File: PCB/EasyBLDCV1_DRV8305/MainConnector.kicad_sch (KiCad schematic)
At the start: 14 parts, among them J1 10159560-A00221RLF, U4 LMR16006XDDCR

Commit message: Fixed Naming Scheme
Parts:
- removed J1: 10159560-A00221RLF, Connectors:AMPHENOL_10159560-A00221RLF, symbol Connectors:10159560-A00221RLF
- removed L1: 15u, symbol Device:L
- removed U4: LMR16006XDDCR, LMR16006XDDCR:DDC0006A, symbol LMR16006XDDCR:LMR16006XDDCR
- added J1: 10159560-A00221RLF, 10159560-A00221RLF:AMPHENOL_10159560-A00221RLF, symbol EasyBLDC:10159560-A00221RLF
- added L1: SD53-120-R, EasyBLDC:SD53, symbol SD53:SD53-470-R
- added U4: LMR16006XDDCR, EasyBLDC:DDC0006A, symbol EasyBLDC:LMR16006XDDCR
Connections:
- net 3.3V: now also L1.2
- net COM: now also J1.10
- net GND: now also J1.3, J1.4, J1.8, J1.9, J1.S1 (SHIELD), J1.S2 (SHIELD__1), U4.2 (GND)
- net MOT_A: now also J1.5
- net MOT_B: now also J1.6
- net MOT_C: now also J1.7
- net PVDD: now also J1.1, J1.2, U4.5 (VIN)
- net at C20.1, D1.1 (K): now also L1.1, U4.6 (SW)
- net at R15.2, R16.1: now also U4.3 (FB)
- net at C20.2: now also U4.1 (CB)

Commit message: Updated Schematic With Missing Footprints
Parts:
- C18: footprint (none) -> EasyBLDC:CAP_FP_10P3X10P3_PAN
- J1: footprint 10159560-A00221RLF:AMPHENOL_10159560-A00221RLF -> EasyBLDC:AMPHENOL_10159560-A00221RLF
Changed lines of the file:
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@@
 			)
 		)
-		(property "Footprint" ""
+		(property "Footprint" "EasyBLDC:CAP_FP_10P3X10P3_PAN"
 			(at 59.69 127 0)
 			(effects
@@
 			)
 		)
-		(property "Footprint" "10159560-A00221RLF:AMPHENOL_10159560-A00221RLF"
+		(property "Footprint" "EasyBLDC:AMPHENOL_10159560-A00221RLF"
 			(at 71.12 60.96 0)
 			(effects

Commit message: Finished Initial Layout
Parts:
- 3V3: footprint TestPoint:TestPoint_Pad_D3.0mm -> TestPoint:TestPoint_Pad_D2.0mm
- C18: value 390u -> 10u; footprint EasyBLDC:CAP_FP_10P3X10P3_PAN -> Capacitor_SMD:C_1210_3225Metric
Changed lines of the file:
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@@
 			)
 		)
-		(property "Value" "390u"
+		(property "Value" "10u"
 			(at 63.5 127.6349 0)
 			(effects
@@
 			)
 		)
-		(property "Footprint" "EasyBLDC:CAP_FP_10P3X10P3_PAN"
+		(property "Footprint" "Capacitor_SMD:C_1210_3225Metric"
 			(at 59.69 127 0)
 			(effects
@@
 			)
 		)
-		(property "Footprint" "TestPoint:TestPoint_Pad_D3.0mm"
+		(property "Footprint" "TestPoint:TestPoint_Pad_D2.0mm"
 			(at 237.49 44.45 0)
 			(effects

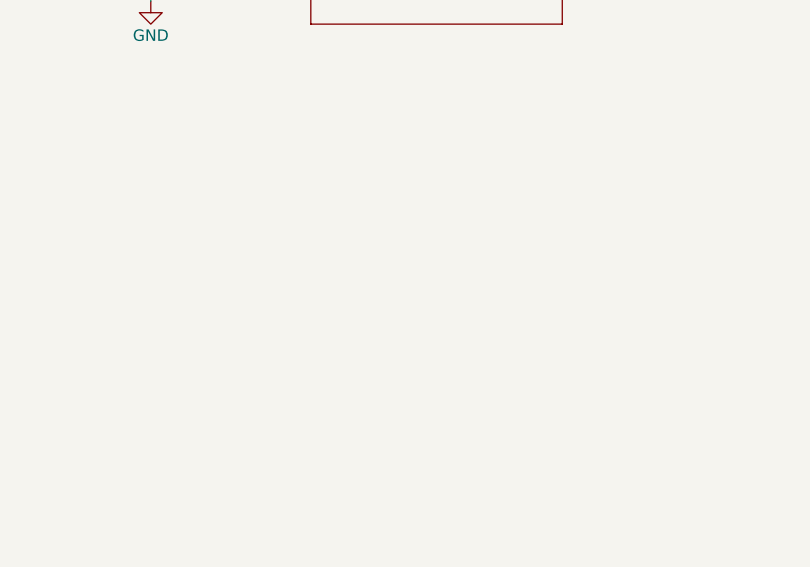
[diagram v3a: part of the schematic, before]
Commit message: Fixed More DRC started final layout
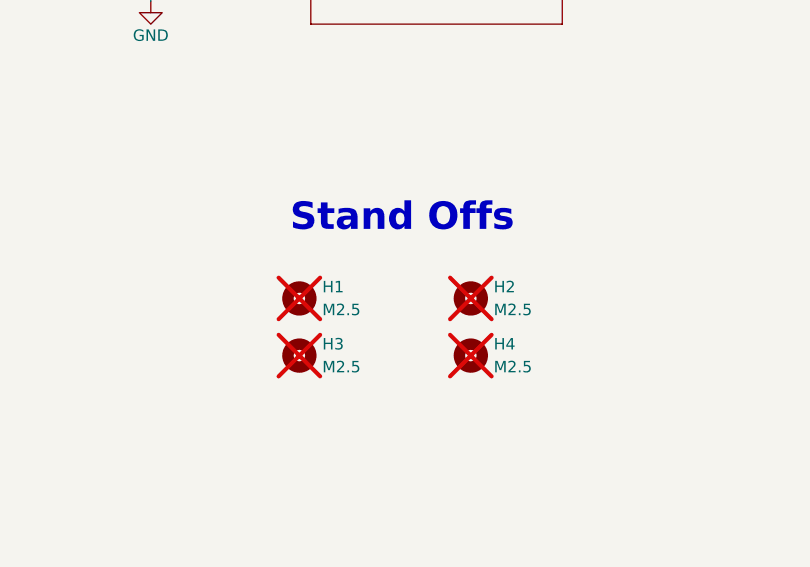
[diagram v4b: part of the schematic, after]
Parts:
- added H1, H2, H3, H4: M2.5, MountingHole:MountingHole_2.7mm_M2.5_DIN965, symbol Mechanical:MountingHole
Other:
- note added: "Stand Offs"

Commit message: Updated PCB Graphics and Layout
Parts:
- H1, H2, H3, H4: footprint MountingHole:MountingHole_2.7mm_M2.5_DIN965 -> MountingHole:MountingHole_2.7mm_M2.5_ISO7380
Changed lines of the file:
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@@
 			)
 		)
-		(property "Footprint" "MountingHole:MountingHole_2.7mm_M2.5_DIN965"
+		(property "Footprint" "MountingHole:MountingHole_2.7mm_M2.5_ISO7380"
 			(at 167.64 120.65 0)
 			(effects
@@
 			)
 		)
-		(property "Footprint" "MountingHole:MountingHole_2.7mm_M2.5_DIN965"
+		(property "Footprint" "MountingHole:MountingHole_2.7mm_M2.5_ISO7380"
 			(at 148.59 114.3 0)
 			(effects
@@
 			)
 		)
-		(property "Footprint" "MountingHole:MountingHole_2.7mm_M2.5_DIN965"
+		(property "Footprint" "MountingHole:MountingHole_2.7mm_M2.5_ISO7380"
 			(at 167.64 114.3 0)
 			(effects
@@
 			)
 		)
-		(property "Footprint" "MountingHole:MountingHole_2.7mm_M2.5_DIN965"
+		(property "Footprint" "MountingHole:MountingHole_2.7mm_M2.5_ISO7380"
 			(at 148.59 120.65 0)
 			(effects
